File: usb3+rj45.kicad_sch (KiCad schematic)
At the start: 63 parts, among them J1 Amphenol_RJE361882415, T1 Choke_SRF2012A-801Y, T2 Choke_SRF2012A-801Y, T3 Choke_SRF2012A-801Y, T4 Choke_SRF2012A-801Y, T5 Trans_SM453229-381N7Y, T6 Trans_SM453229-381N7Y, T7 Trans_SM453229-381N7Y, T8 Trans_SM453229-381N7Y, U1 ESD204DQAR, U2 ESD204DQAR, U3 AP22615A_TSOT26, U4 AP22615A_TSOT26

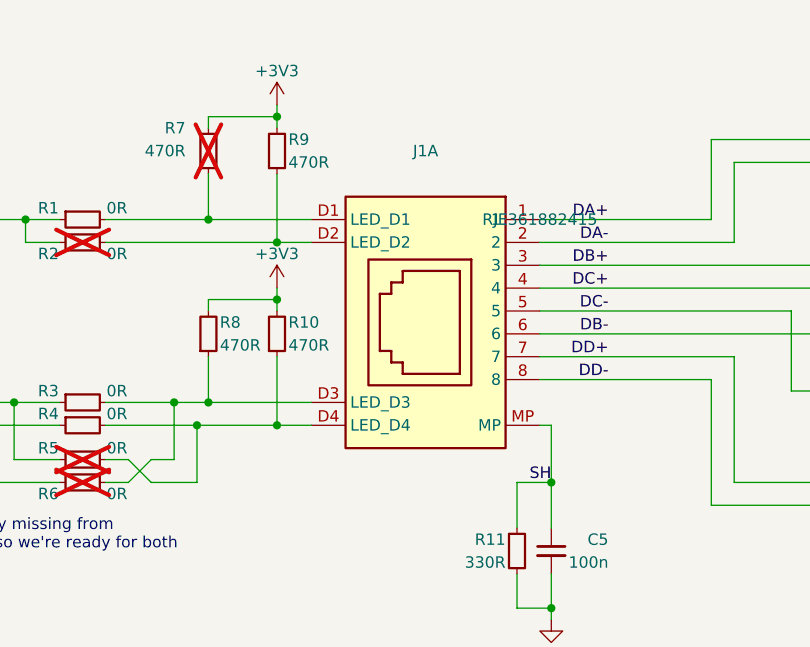
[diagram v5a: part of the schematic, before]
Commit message: [#65447] Fix rotated LEDs, overlapping text and symbols, add rules
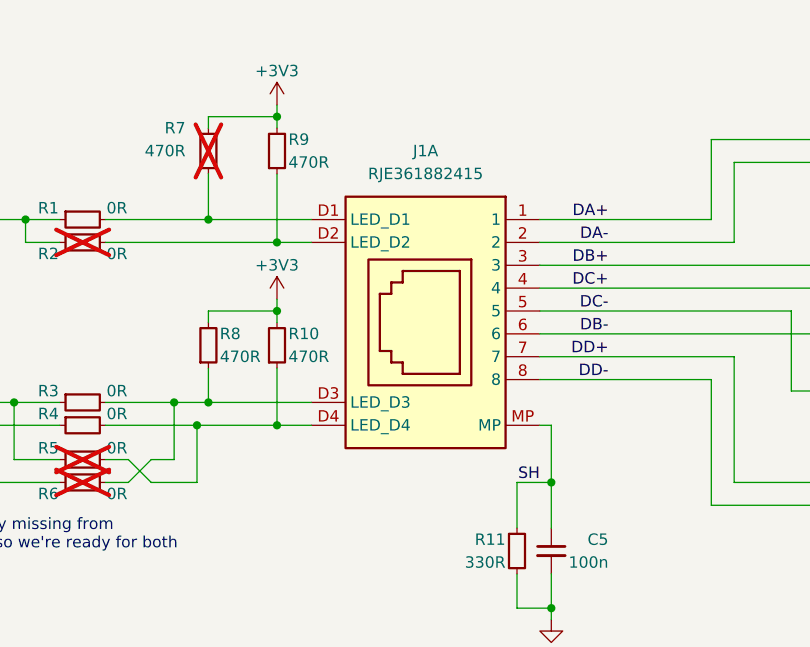
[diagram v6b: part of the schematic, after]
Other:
- moved on the sheet: R10, R8
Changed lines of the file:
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@@
   (junction (at 204.47 165.1) (diameter 0) (color 0 0 0 0)
   )
-  (junction (at 133.35 72.39) (diameter 0) (color 0 0 0 0)
+  (junction (at 133.35 73.66) (diameter 0) (color 0 0 0 0)
   )
   (junction (at 233.68 227.33) (diameter 0) (color 0 0 0 0)
@@
     (stroke (width 0) (type default))
   )
-  (wire (pts (xy 162.56 86.36) (xy 163.83 86.36))
+  (wire (pts (xy 163.83 86.36) (xy 162.56 86.36))
     (stroke (width 0) (type default))
   )
@@
     (stroke (width 0) (type default))
   )
-  (wire (pts (xy 125.73 72.39) (xy 133.35 72.39))
+  (wire (pts (xy 125.73 73.66) (xy 133.35 73.66))
     (stroke (width 0) (type default))
   )
@@
     (stroke (width 0) (type default))
   )
-  (wire (pts (xy 125.73 73.66) (xy 125.73 72.39))
+  (wire (pts (xy 125.73 74.93) (xy 125.73 73.66))
     (stroke (width 0) (type default))
   )
@@
     (stroke (width 0) (type default))
   )
-  (wire (pts (xy 133.35 78.74) (xy 133.35 86.36))
+  (wire (pts (xy 133.35 80.01) (xy 133.35 86.36))
     (stroke (width 0) (type default))
   )
@@
     (stroke (width 0) (type default))
   )
-  (wire (pts (xy 133.35 71.12) (xy 133.35 72.39))
+  (wire (pts (xy 133.35 72.39) (xy 133.35 73.66))
     (stroke (width 0) (type default))
   )
@@
     (stroke (width 0) (type default))
   )
-  (wire (pts (xy 125.73 78.74) (xy 125.73 83.82))
+  (wire (pts (xy 125.73 80.01) (xy 125.73 83.82))
     (stroke (width 0) (type default))
   )
-  (wire (pts (xy 133.35 72.39) (xy 133.35 73.66))
+  (wire (pts (xy 133.35 73.66) (xy 133.35 74.93))
     (stroke (width 0) (type default))
   )
@@
     (effects (font (size 1.27 1.27)) (justify left bottom))
   )
+  (label "SH" (at 162.56 92.71 180) (fields_autoplaced)
+    (effects (font (size 1.27 1.27)) (justify right bottom))
+  )
   (label "FLG_1B" (at 229.87 157.48 180) (fields_autoplaced)
     (effects (font (size 1.27 1.27)) (justify right bottom))
@@
     (effects (font (size 1.27 1.27)) (justify left bottom))
   )
-  (label "SH" (at 163.83 92.71 180) (fields_autoplaced)
-    (effects (font (size 1.27 1.27)) (justify right bottom))
-  )
   (label "DD-" (at 170.18 81.28 180) (fields_autoplaced)
     (effects (font (size 1.27 1.27)) (justify right bottom))
@@
     )
   )
-  (symbol (lib_id "antmicropower:+3V3") (at 133.35 71.12 0) (unit 1)
+  (symbol (lib_id "antmicropower:+3V3") (at 133.35 72.39 0) (unit 1)
     (in_bom yes) (on_board yes) (dnp no)
-    (property "Reference" "#PWR02" (at 148.59 71.12 0)
+    (property "Reference" "#PWR02" (at 148.59 72.39 0)
       (effects (font (size 1.27 1.27) (thickness 0.15)) (justify left bottom) hide)
     )
-    (property "Value" "+3V3" (at 133.35 67.31 0)
+    (property "Value" "+3V3" (at 133.35 68.58 0)
       (effects (font (size 1.27 1.27) (thickness 0.15)))
     )
-    (property "Footprint" "" (at 148.59 78.74 0)
+    (property "Footprint" "" (at 148.59 80.01 0)
       (effects (font (size 1.27 1.27) (thickness 0.15)) (justify left bottom) hide)
     )
-    (property "Datasheet" "" (at 148.59 81.28 0)
+    (property "Datasheet" "" (at 148.59 82.55 0)
       (effects (font (size 1.27 1.27) (thickness 0.15)) (justify left bottom) hide)
     )
-    (property "Author" "Antmicro" (at 148.59 73.66 0)
+    (property "Author" "Antmicro" (at 148.59 74.93 0)
       (effects (font (size 1.27 1.27) (thickness 0.15)) (justify left bottom) hide)
     )
-    (property "License" "Apache-2.0" (at 148.59 76.2 0)
+    (property "License" "Apache-2.0" (at 148.59 77.47 0)
       (effects (font (size 1.27 1.27) (thickness 0.15)) (justify left bottom) hide)
     )
@@
     )
   )
-  (symbol (lib_id "antmicroResistors0402:R_470R_0402") (at 133.35 78.74 90) (unit 1)
+  (symbol (lib_id "antmicroResistors0402:R_470R_0402") (at 133.35 80.01 90) (unit 1)
     (in_bom yes) (on_board yes) (dnp no)
-    (property "Reference" "R10" (at 134.62 74.93 90)
+    (property "Reference" "R10" (at 134.62 76.2 90)
       (effects (font (size 1.27 1.27) (thickness 0.15)) (justify right))
     )
-    (property "Value" "R_470R_0402" (at 146.05 58.42 0)
+    (property "Value" "R_470R_0402" (at 146.05 59.69 0)
       (effects (font (size 1.27 1.27) (thickness 0.15)) (justify left bottom) hide)
     )
-    (property "Footprint" "antmicro-footprints:R_0402_1005Metric" (at 148.59 58.42 0)
+    (property "Footprint" "antmicro-footprints:R_0402_1005Metric" (at 148.59 59.69 0)
       (effects (font (size 1.27 1.27) (thickness 0.15)) (justify left bottom) hide)
     )
-    (property "Datasheet" "https://www.bourns.com/docs/product-datasheets/cr.pdf" (at 151.13 58.42 0)
+    (property "Datasheet" "https://www.bourns.com/docs/product-datasheets/cr.pdf" (at 151.13 59.69 0)
       (effects (font (size 1.27 1.27) (thickness 0.15)) (justify left bottom) hide)
     )
-    (property "MPN" "CR0402-FX-4700GLF" (at 153.67 58.42 0)
+    (property "MPN" "CR0402-FX-4700GLF" (at 153.67 59.69 0)
       (effects (font (size 1.27 1.27) (thickness 0.15)) (justify left bottom) hide)
     )
-    (property "Manufacturer" "Bourns" (at 156.21 58.42 0)
+    (property "Manufacturer" "Bourns" (at 156.21 59.69 0)
       (effects (font (size 1.27 1.27) (thickness 0.15)) (justify left bottom) hide)
     )
-    (property "License" "Apache-2.0" (at 158.75 58.42 0)
+    (property "License" "Apache-2.0" (at 158.75 59.69 0)
       (effects (font (size 1.27 1.27) (thickness 0.15)) (justify left bottom) hide)
     )
-    (property "Author" "Antmicro" (at 161.29 58.42 0)
+    (property "Author" "Antmicro" (at 161.29 59.69 0)
       (effects (font (size 1.27 1.27) (thickness 0.15)) (justify left bottom) hide)
     )
-    (property "Val" "470R" (at 134.62 77.47 90)
+    (property "Val" "470R" (at 134.62 78.74 90)
       (effects (font (size 1.27 1.27) (thickness 0.15)) (justify right))
     )
-    (property "Tolerance" "1%" (at 143.51 58.42 0)
+    (property "Tolerance" "1%" (at 143.51 59.69 0)
       (effects (font (size 1.27 1.27)) (justify left bottom) hide)
     )
-    (property "Public" "False" (at 163.83 58.42 0)
+    (property "Public" "False" (at 163.83 59.69 0)
       (effects (font (size 1.27 1.27)) (justify left bottom) hide)
     )
@@
     )
   )
-  (symbol (lib_id "antmicroResistors0402:R_470R_0402") (at 125.73 78.74 90) (unit 1)
+  (symbol (lib_id "antmicroResistors0402:R_470R_0402") (at 125.73 80.01 90) (unit 1)
     (in_bom yes) (on_board yes) (dnp no)
-    (property "Reference" "R8" (at 127 74.93 90)
+    (property "Reference" "R8" (at 127 76.2 90)
       (effects (font (size 1.27 1.27) (thickness 0.15)) (justify right))
     )
-    (property "Value" "R_470R_0402" (at 138.43 58.42 0)
+    (property "Value" "R_470R_0402" (at 138.43 59.69 0)
       (effects (font (size 1.27 1.27) (thickness 0.15)) (justify left bottom) hide)
     )
-    (property "Footprint" "antmicro-footprints:R_0402_1005Metric" (at 140.97 58.42 0)
+    (property "Footprint" "antmicro-footprints:R_0402_1005Metric" (at 140.97 59.69 0)
       (effects (font (size 1.27 1.27) (thickness 0.15)) (justify left bottom) hide)
     )
-    (property "Datasheet" "https://www.bourns.com/docs/product-datasheets/cr.pdf" (at 143.51 58.42 0)
+    (property "Datasheet" "https://www.bourns.com/docs/product-datasheets/cr.pdf" (at 143.51 59.69 0)
       (effects (font (size 1.27 1.27) (thickness 0.15)) (justify left bottom) hide)
     )
-    (property "MPN" "CR0402-FX-4700GLF" (at 146.05 58.42 0)
+    (property "MPN" "CR0402-FX-4700GLF" (at 146.05 59.69 0)
       (effects (font (size 1.27 1.27) (thickness 0.15)) (justify left bottom) hide)
     )
-    (property "Manufacturer" "Bourns" (at 148.59 58.42 0)
+    (property "Manufacturer" "Bourns" (at 148.59 59.69 0)
       (effects (font (size 1.27 1.27) (thickness 0.15)) (justify left bottom) hide)
     )
-    (property "License" "Apache-2.0" (at 151.13 58.42 0)
+    (property "License" "Apache-2.0" (at 151.13 59.69 0)
       (effects (font (size 1.27 1.27) (thickness 0.15)) (justify left bottom) hide)
     )
-    (property "Author" "Antmicro" (at 153.67 58.42 0)
+    (property "Author" "Antmicro" (at 153.67 59.69 0)
       (effects (font (size 1.27 1.27) (thickness 0.15)) (justify left bottom) hide)
     )
-    (property "Val" "470R" (at 127 77.47 90)
+    (property "Val" "470R" (at 127 78.74 90)
       (effects (font (size 1.27 1.27) (thickness 0.15)) (justify right))
     )
-    (property "Tolerance" "1%" (at 135.89 58.42 0)
+    (property "Tolerance" "1%" (at 135.89 59.69 0)
       (effects (font (size 1.27 1.27)) (justify left bottom) hide)
     )
-    (property "Public" "False" (at 156.21 58.42 0)
+    (property "Public" "False" (at 156.21 59.69 0)
       (effects (font (size 1.27 1.27)) (justify left bottom) hide)
     )
@@
   )
   (symbol (lib_id "antmicroModularConnectorsJacks:Amphenol_RJE361882415") (at 162.56 63.5 0) (mirror y) (unit 1)
-    (in_bom yes) (on_board yes) (dnp no) (fields_autoplaced)
+    (in_bom yes) (on_board yes) (dnp no)
     (property "Reference" "J1" (at 149.86 55.88 0)
       (effects (font (size 1.27 1.27)))
@@
       (effects (font (size 1.27 1.27)) hide)
     )
-    (property "MPN" "RJE361882415" (at 162.56 63.5 0)
+    (property "MPN" "RJE361882415" (at 149.86 58.42 0)
       (effects (font (size 1.27 1.27)))
     )

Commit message: [#65840] Roughly route PCIe, GbE
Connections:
- net DC_FL+: now reaches T3.1, T7.1
- net DC_FL-: now reaches T3.4, T7.2
- net DD_FL+: now reaches T4.1, T8.1
- net DD_FL-: now reaches T4.4, T8.2
- net DA_FL+: now reaches T1.1, T5.1
- net DA_FL-: now reaches T1.4, T5.2
- net DB_FL+: now reaches T2.1, T6.1
- net DB_FL-: now reaches T2.4, T6.2
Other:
- moved on the sheet: C12, C13, C14, C15, C18, R14, R15, R16, R17, R30, T5, T6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

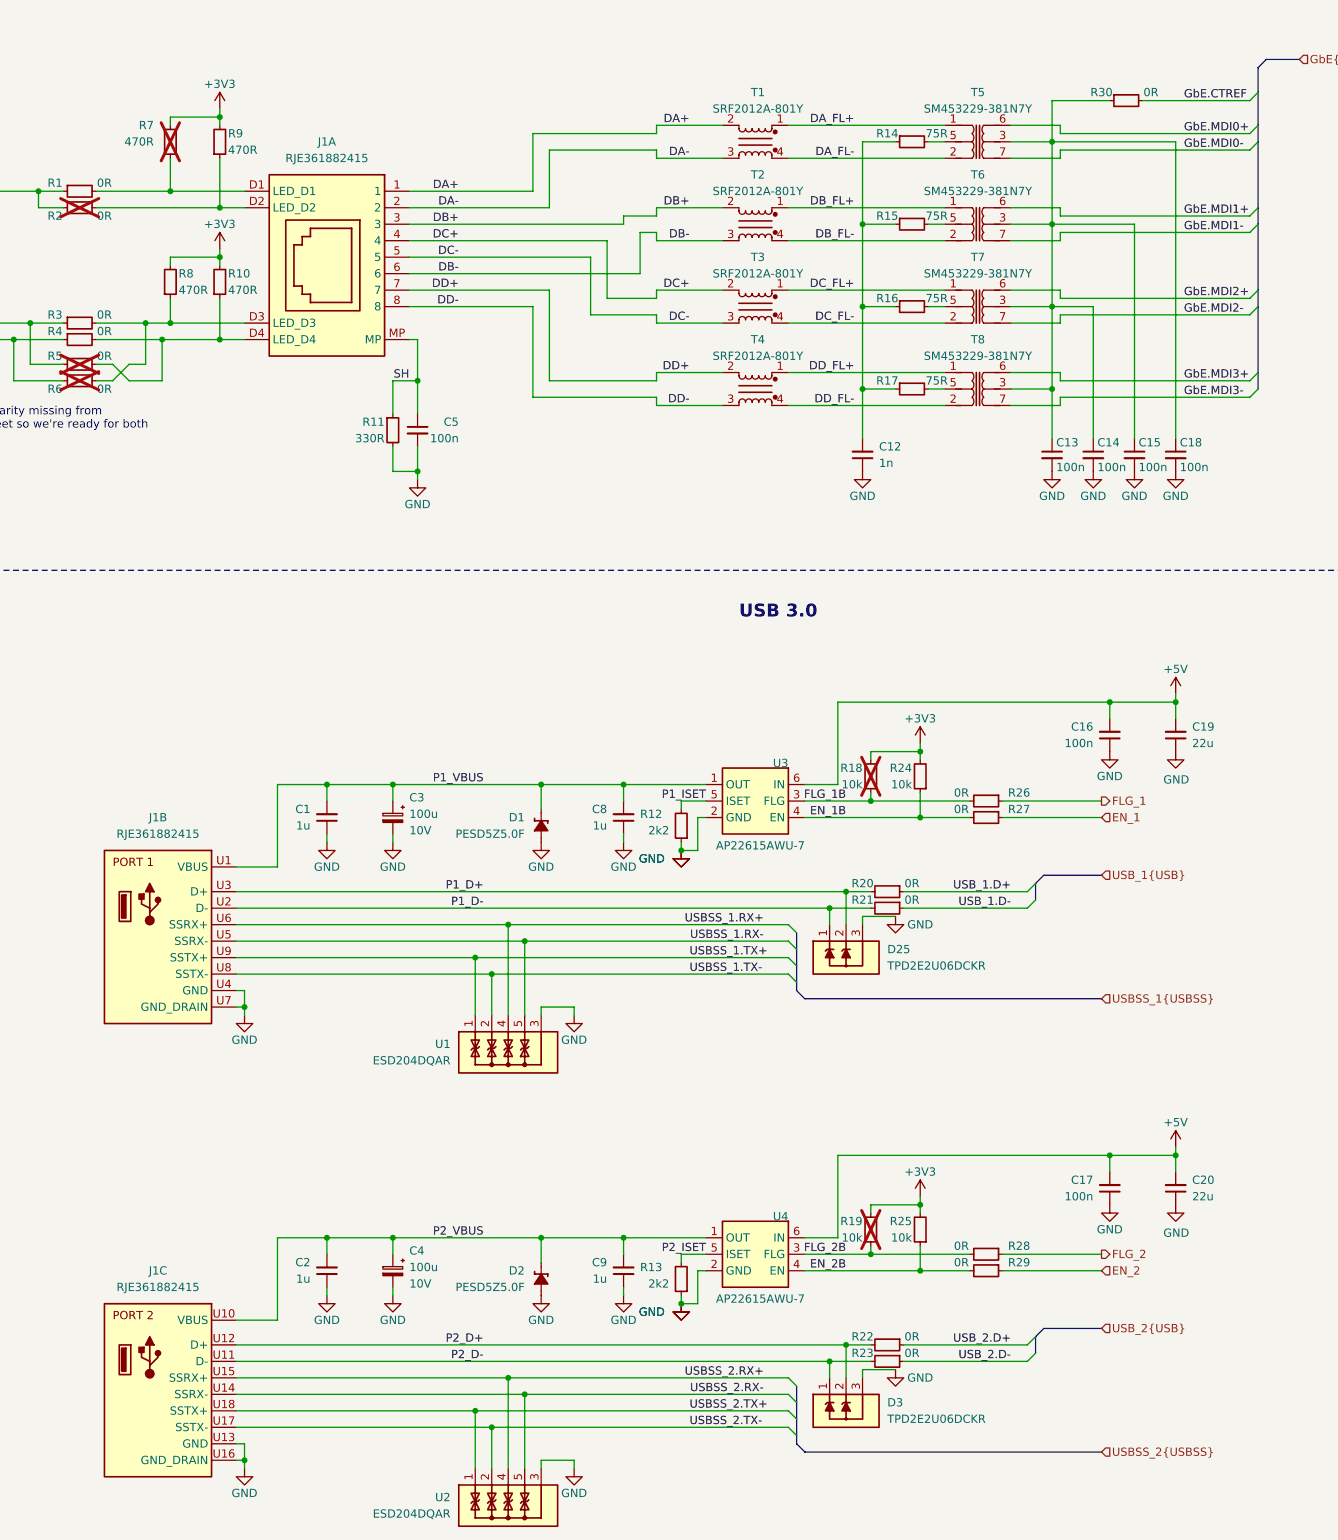
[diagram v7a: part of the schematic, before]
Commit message: [#66613] Fix ERC, adjust overlapping text on schematic
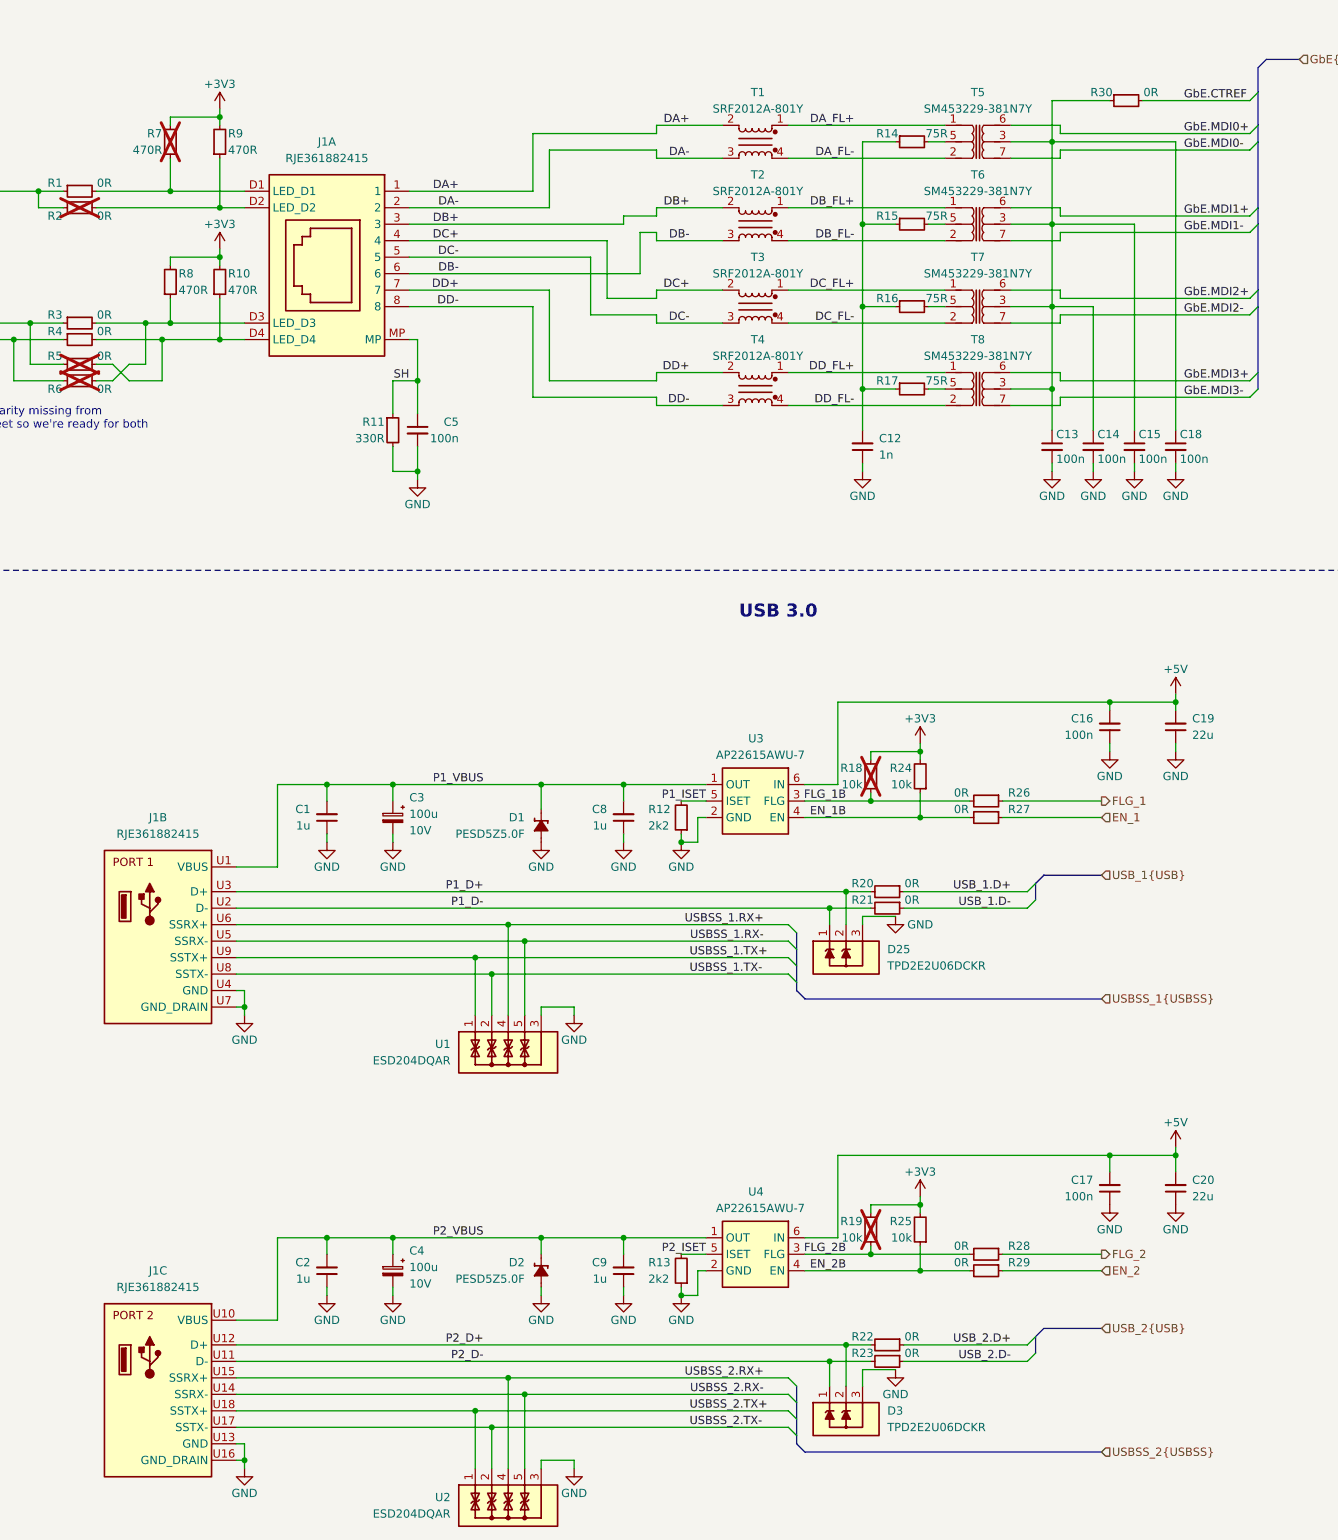
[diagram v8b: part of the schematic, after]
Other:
- moved on the sheet: C12, C13, C14, C15, C16, C18, C19, D2, D3, R12, R13
